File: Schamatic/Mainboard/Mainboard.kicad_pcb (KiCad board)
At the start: 2 copper layers, 45 x 130 mm, 277 parts, among them J1 CONN_01X02, J10 CONN_01X04, J2 CONN_01X02, J3 CONN_01X02, J4 CONN_01X02, J5 CONN_01X02, J6 CONN_02X05, J7 CONN_02X20, J8 CONN_01X02, J9 CONN_01X02, Q1 Q_NMOS_GDS, Q2 PSMN014-40YS, U1 LM2678-3.3V, U10 LTC2954, U2 LM2678-5V, U3 MC78M00, U4 LM5122, U5 UCC27611, U6 ACS781, U7 LSM6DS33, U8 STM32F031G6U6, U9 LTC2876, Y1 Resonator_Small

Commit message: changes
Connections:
- Y1 pad 2: (no net) -> Earth
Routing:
- net +BATT: track 200.3 -> 195.4 mm
- net 3.3V: track 250.1 -> 250.6 mm
- net Earth: vias 0 -> 1
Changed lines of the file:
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@@
 (kicad_pcb (version 4) (host pcbnew 4.0.6)
   (general
-    (links 0)
-    (no_connects 1)
-    (area 44.8 37.5 99.558572 172.600001)
+    (links 460)
+    (no_connects 2)
+    (area 49.924999 39.924999 95.075001 170.075001)
     (thickness 1.6)
     (drawings 4)
-    (tracks 1029)
+    (tracks 1034)
     (zones 0)
     (modules 277)
@@
     (47 F.CrtYd user)
     (48 B.Fab user)
-    (49 F.Fab user hide)
+    (49 F.Fab user)
   )
   (setup
-    (last_trace_width 0.13)
+    (last_trace_width 0.25)
     (user_trace_width 0.13)
     (user_trace_width 0.25)
@@
     (pad 1 smd rect (at 0 2.3 270) (size 0.4 1.4) (layers F.Cu F.Paste F.Mask)
       (net 50 "Net-(U8-Pad2)"))
-    (pad 2 smd rect (at 1.2 2.3 270) (size 0.4 1.4) (layers F.Cu F.Paste F.Mask))
+    (pad 2 smd rect (at 1.2 2.3 270) (size 0.4 1.4) (layers F.Cu F.Paste F.Mask)
+      (net 1 Earth))
     (pad 3 smd rect (at 2.4 2.3 270) (size 0.4 1.4) (layers F.Cu F.Paste F.Mask)
       (net 51 "Net-(U8-Pad3)"))
@@
   (gr_line (start 95 40) (end 95 170) (layer Edge.Cuts) (width 0.15))
   (gr_line (start 50 40) (end 95 40) (layer Edge.Cuts) (width 0.15))
+  (via (at 59.3 69.5) (size 0.4) (drill 0.25) (layers F.Cu B.Cu) (net 1))
   (segment (start 74.5 149.8) (end 74.5 149.58) (width 0.13) (layer F.Cu) (net 1))
   (segment (start 74.5 149.58) (end 74.8 149.28) (width 0.13) (layer F.Cu) (net 1))
@@
   (segment (start 58.725 149.5) (end 59.615 150.39) (width 0.25) (layer F.Cu) (net 3))
   (segment (start 59.615 150.39) (end 60.4 150.39) (width 0.25) (layer F.Cu) (net 3))
+  (segment (start 53.4 157.7) (end 53.4 144.75) (width 2) (layer B.Cu) (net 4))
+  (segment (start 53.4 144.75) (end 53.4 110.6) (width 2) (layer B.Cu) (net 4))
+  (segment (start 59.5 144.8) (end 53.45 144.8) (width 0.25) (layer B.Cu) (net 4))
+  (segment (start 53.45 144.8) (end 53.4 144.75) (width 0.25) (layer B.Cu) (net 4))
   (segment (start 88.4 113.6) (end 77.834602 113.6) (width 0.13) (layer F.Cu) (net 4))
   (segment (start 73.345001 113.645001) (end 70.499999 110.799999) (width 0.13) (layer F.Cu) (net 4))
@@
   (via (at 53.4 108.6) (size 0.4) (drill 0.25) (layers F.Cu B.Cu) (net 4))
   (via (at 53.4 109.6) (size 0.4) (drill 0.25) (layers F.Cu B.Cu) (net 4))
-  (segment (start 59.5 144.8) (end 53.2 138.5) (width 0.13) (layer B.Cu) (net 4))
-  (segment (start 53.2 138.5) (end 53.2 136.4) (width 0.13) (layer B.Cu) (net 4))
   (segment (start 64.22 144.28) (end 63.654999 144.845001) (width 0.13) (layer F.Cu) (net 4))
   (segment (start 63.654999 144.845001) (end 59.545001 144.845001) (width 0.13) (layer F.Cu) (net 4))
@@
   (segment (start 70.3 106) (end 70.2 105.9) (width 2) (layer F.Cu) (net 4))
   (via (at 70.3 110.6) (size 0.4) (drill 0.25) (layers F.Cu B.Cu) (net 4))
-  (segment (start 53.4 157.7) (end 53.4 110.6) (width 2) (layer B.Cu) (net 4))
   (via (at 53.4 110.6) (size 0.4) (drill 0.25) (layers F.Cu B.Cu) (net 4))
   (segment (start 61.5 165.8) (end 53.4 157.7) (width 2) (layer B.Cu) (net 4))
@@
   (segment (start 74.1 144.7) (end 74.1 146.4) (width 0.25) (layer F.Cu) (net 12))
   (segment (start 74.1 146.4) (end 74 146.5) (width 0.25) (layer F.Cu) (net 12))
+  (segment (start 78 97.6) (end 76.5 97.6) (width 0.25) (layer F.Cu) (net 13))
+  (segment (start 76.5 97.6) (end 76.05 98.05) (width 0.25) (layer F.Cu) (net 13))
+  (segment (start 76.05 98.05) (end 76.05 101.05) (width 0.25) (layer F.Cu) (net 13))
+  (segment (start 76.05 101.05) (end 75.4 101.7) (width 0.25) (layer F.Cu) (net 13))
+  (segment (start 75.4 101.7) (end 75.4 101.9) (width 0.25) (layer F.Cu) (net 13))
   (segment (start 85.119999 99.414978) (end 83.70502 97.999999) (width 0.25) (layer F.Cu) (net 13))
   (segment (start 88.9 103.35) (end 86.425001 100.875001) (width 0.25) (layer F.Cu) (net 13))
@@
   (segment (start 65.785161 75.799991) (end 64.93018 74.94501) (width 0.5) (layer B.Cu) (net 13))
   (segment (start 78 97.6) (end 77.7 97.6) (width 0.5) (layer F.Cu) (net 13))
-  (segment (start 77.7 97.6) (end 76.5 98.8) (width 0.5) (layer F.Cu) (net 13))
-  (segment (start 76.5 98.8) (end 76.5 101.5) (width 0.5) (layer F.Cu) (net 13))
-  (segment (start 76.5 101.5) (end 76.1 101.9) (width 0.5) (layer F.Cu) (net 13))
-  (segment (start 76.1 101.9) (end 75.4 101.9) (width 0.5) (layer F.Cu) (net 13))
   (segment (start 80.45 90.8) (end 80.45 85.91) (width 2) (layer F.Cu) (net 13))
   (segment (start 80.45 85.91) (end 77.84 83.3) (width 2) (layer F.Cu) (net 13))
@@
   (segment (start 75.7 62.035) (end 75.7 62.6) (width 0.5) (layer F.Cu) (net 13))
   (segment (start 88.025 72.18) (end 86.95 72.18) (width 0.5) (layer F.Cu) (net 13))
+  (segment (start 59.7 100.45) (end 59.594999 100.555001) (width 0.25) (layer F.Cu) (net 14))
+  (segment (start 59.594999 100.555001) (end 59.594999 100.905001) (width 0.25) (layer F.Cu) (net 14))
+  (segment (start 59.594999 100.905001) (end 58.8 101.7) (width 0.25) (layer F.Cu) (net 14))
   (segment (start 61.1 98.3) (end 61.1 99.05) (width 0.25) (layer F.Cu) (net 14))
   (segment (start 61.1 99.05) (end 59.7 100.45) (width 0.25) (layer F.Cu) (net 14))
-  (segment (start 59.7 100.8) (end 58.8 101.7) (width 0.25) (layer F.Cu) (net 14))
-  (segment (start 59.7 100.45) (end 59.7 100.8) (width 0.25) (layer F.Cu) (net 14))
   (segment (start 58.8 101.7) (end 58.8 101.9) (width 0.25) (layer F.Cu) (net 14))
   (segment (start 64.8 90.8) (end 64.8 86.3) (width 2) (layer F.Cu) (net 14))
@@
   (segment (start 89.25 108.05) (end 90.7 106.6) (width 0.13) (layer F.Cu) (net 56))
   (segment (start 90.7 106.6) (end 90.9 106.6) (width 0.13) (layer F.Cu) (net 56))
+  (segment (start 75.4 97.3) (end 75.85 97.75) (width 0.13) (layer B.Cu) (net 57))
+  (segment (start 75.85 97.75) (end 75.85 108.85) (width 0.13) (layer B.Cu) (net 57))
+  (segment (start 75.85 108.85) (end 72.899999 111.800001) (width 0.13) (layer B.Cu) (net 57))
+  (segment (start 72.899999 111.800001) (end 72.7 112) (width 0.13) (layer B.Cu) (net 57))
   (segment (start 85.545002 112.689602) (end 85.334605 112.899999) (width 0.13) (layer F.Cu) (net 57))
-  (segment (start 75.4 97.3) (end 75.4 109.3) (width 0.13) (layer B.Cu) (net 57))
   (segment (start 87.774206 107.589602) (end 86.895002 107.589602) (width 0.13) (layer F.Cu) (net 57))
   (segment (start 88.25 108.065396) (end 87.774206 107.589602) (width 0.13) (layer F.Cu) (net 57))
-  (segment (start 72.899999 111.800001) (end 72.7 112) (width 0.13) (layer B.Cu) (net 57))
-  (segment (start 75.4 109.3) (end 72.899999 111.800001) (width 0.13) (layer B.Cu) (net 57))
   (segment (start 88.25 109.2) (end 88.25 108.065396) (width 0.13) (layer F.Cu) (net 57))
   (segment (start 72.500001 112.199999) (end 72.7 112) (width 0.13) (layer B.Cu) (net 57))

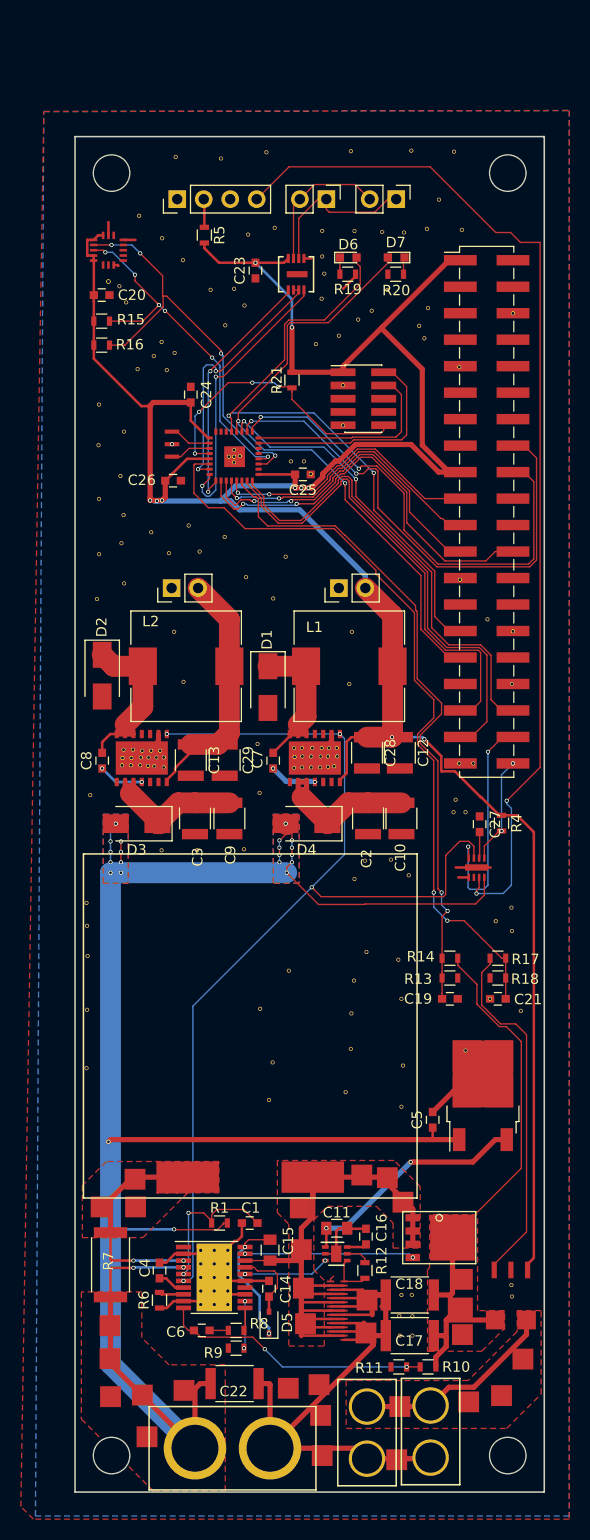
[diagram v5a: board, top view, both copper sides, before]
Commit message: mainboard plain MOSFETS
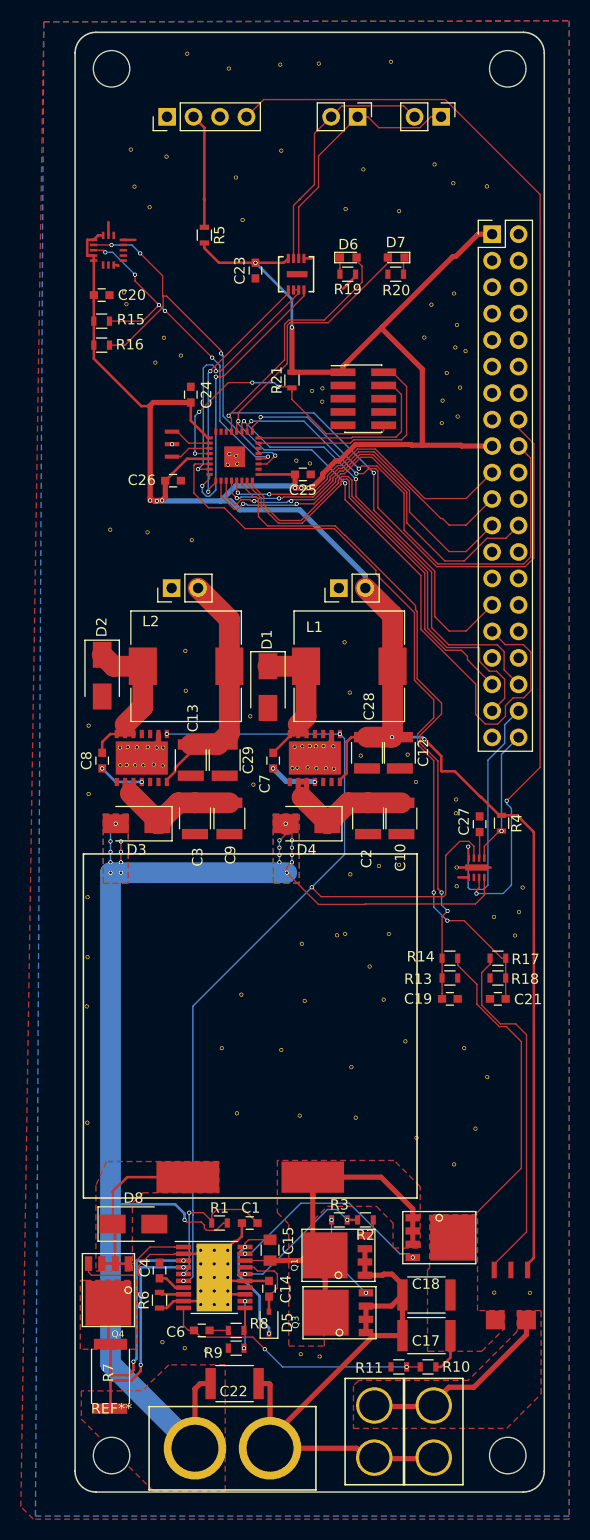
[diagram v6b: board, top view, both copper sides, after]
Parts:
- removed ? (x30): , Dizzy:2x2mm-pad
- removed C11: 2uF, Capacitors_SMD:C_0805
- removed C16: 2uF, Capacitors_SMD:C_0603
- removed C5: 1uF, Capacitors_SMD:C_0603
- removed R12: 10Ohm, Resistors_SMD:R_0603
- removed the REF** at (70.8, 71.2)
- removed the REF** at (51.2, 129.3)
- removed the REF** at (54.8, 98.8)
- removed the REF** at (55.6, 98.8)
- removed the REF** at (56.5, 98.9)
- removed the REF** at (57.4, 98.9)
- removed the REF** at (58.2, 98.9)
- removed the REF** at (75.0, 100.4)
- removed the REF** at (74.3, 100.5)
- removed the REF** at (73.6, 100.5)
- removed the REF** at (72.8, 100.5)
- removed the REF** at (71.8, 100.5)
- removed the REF** at (51.2, 123.8)
- removed the REF** at (71.1, 100.5)
- removed the REF** at (71.2, 99.5)
- removed the REF** at (71.9, 99.5)
- removed the REF** at (72.8, 99.5)
- removed the REF** at (73.7, 99.5)
- removed the REF** at (74.3, 99.5)
- removed the REF** at (75.2, 99.5)
- removed the REF** at (75.2, 98.7)
- removed the REF** at (74.5, 98.7)
- removed the REF** at (73.8, 98.7)
- removed the REF** at (51.3, 118.6)
- removed the REF** at (72.8, 98.7)
- removed the REF** at (71.8, 98.7)
- removed the REF** at (71.1, 98.7)
- removed the REF** at (87.0, 82.5)
- removed the REF** at (89.7, 86.3)
- removed the REF** at (92.1, 87.5)
- removed the REF** at (92.0, 92.5)
- removed the REF** at (88.3, 100.1)
- removed the REF** at (87.0, 100.1)
- removed the REF** at (87.5, 104.8)
- removed the REF** at (51.2, 115.7)
- removed the REF** at (86.6, 103.6)
- removed the REF** at (86.4, 104.8)
- removed the REF** at (82.1, 110.8)
- removed the REF** at (80.4, 109.3)
- removed the REF** at (77.9, 109.5)
- removed the REF** at (76.9, 111.2)
- removed the REF** at (92.0, 114.0)
- removed the REF** at (90.5, 115.2)
- removed the REF** at (92.0, 116.2)
- removed the REF** at (92.8, 123.8)
- removed the REF** at (51.2, 113.5)
- removed the REF** at (89.9, 122.7)
- removed the REF** at (70.6, 120.0)
- removed the REF** at (67.8, 123.7)
- removed the REF** at (69.0, 128.8)
- removed the REF** at (68.7, 132.4)
- removed the REF** at (76.0, 131.7)
- removed the REF** at (76.5, 127.5)
- removed the REF** at (76.6, 124.1)
- removed the REF** at (78.0, 118.2)
- removed the REF** at (81.1, 119.0)
- removed the REF** at (66.3, 108.3)
- removed the REF** at (76.8, 121.0)
- removed the REF** at (81.4, 122.7)
- removed the REF** at (81.5, 129.1)
- removed the REF** at (81.4, 133.1)
- removed the REF** at (81.2, 153.1)
- removed the REF** at (82.5, 153.2)
- removed the REF** at (82.5, 155.0)
- removed the REF** at (81.2, 155.0)
- removed the REF** at (82.4, 151.1)
- removed the REF** at (81.4, 151.1)
- removed the REF** at (61.8, 108.5)
- removed the REF** at (92.0, 151.2)
- removed the REF** at (92.0, 150.2)
- removed the REF** at (91.5, 43.5)
- removed the REF** at (53.5, 43.5)
- removed the REF** at (87.5, 127.7)
- removed the REF** at (58.4, 108.5)
- removed the REF** at (67.8, 103.0)
- removed the REF** at (67.6, 98.2)
- removed the REF** at (72.0, 71.2)
- removed the REF** at (76.4, 92.5)
- removed the REF** at (76.7, 87.5)
- removed the REF** at (59.6, 87.5)
- removed the REF** at (60.5, 92.3)
- removed the REF** at (69.1, 84.3)
- removed the REF** at (70.3, 80.3)
- removed the REF** at (66.5, 82.2)
- removed the REF** at (62.0, 79.8)
- removed the REF** at (59.1, 80.0)
- removed the REF** at (64.5, 78.4)
- removed the REF** at (72.7, 72.3)
- removed the REF** at (61.0, 77.3)
- removed the REF** at (57.4, 78.0)
- removed the REF** at (54.8, 68.3)
- removed the REF** at (54.5, 72.5)
- removed the REF** at (54.8, 76.3)
- removed the REF** at (54.5, 79.0)
- removed the REF** at (54.8, 82.8)
- removed the REF** at (52.2, 84.3)
- removed the REF** at (52.4, 80.0)
- removed the REF** at (52.4, 74.8)
- removed the REF** at (87.0, 62.1)
- removed the REF** at (52.4, 69.6)
- removed the REF** at (52.4, 65.7)
- removed the REF** at (57.6, 61.0)
- removed the REF** at (59.6, 60.8)
- removed the REF** at (56.1, 62.3)
- removed the REF** at (58.9, 62.4)
- removed the REF** at (58.4, 59.7)
- removed the REF** at (53.3, 53.9) (x2)
- removed the REF** at (54.4, 54.4)
- removed the REF** at (92.1, 57.0)
- removed the REF** at (55.0, 55.9)
- removed the REF** at (86.5, 41.5)
- removed the REF** at (82.3, 41.4)
- removed the REF** at (76.5, 41.4)
- removed the REF** at (68.5, 41.5)
- removed the REF** at (64.1, 42.1)
- removed the REF** at (59.8, 42.0)
- removed the REF** at (56.2, 47.6)
- removed the REF** at (69.2, 48.8)
- removed the REF** at (66.7, 49.4)
- removed the REF** at (84.0, 56.5)
- removed the REF** at (58.5, 49.8)
- removed the REF** at (60.5, 51.9)
- removed the REF** at (63.1, 54.7)
- removed the REF** at (65.3, 54.6)
- removed the REF** at (66.3, 56.2)
- removed the REF** at (64.5, 58.1)
- removed the REF** at (87.2, 49.0)
- removed the REF** at (85.0, 46.0)
- removed the REF** at (83.8, 48.9)
- removed the REF** at (81.7, 49.2)
- removed the REF** at (83.6, 59.4)
- removed the REF** at (79.5, 49.1)
- removed the REF** at (76.9, 49.0)
- removed the REF** at (73.8, 49.0)
- removed the REF** at (73.8, 51.5)
- removed the REF** at (74.0, 53.1)
- removed the REF** at (73.8, 55.5)
- removed the REF** at (73.2, 59.9)
- removed the REF** at (75.4, 59.1)
- removed the REF** at (77.2, 57.5)
- removed the REF** at (78.5, 56.7)
- removed the REF** at (83.1, 58.1)
- removed the REF** at (80.0, 54.7)
- removed the REF** at (75.8, 67.7)
- removed the REF** at (75.8, 63.9)
- removed the REF** at (65.3, 70.0)
- removed the REF** at (65.3, 71.2)
- removed the REF** at (65.9, 70.7)
- removed the REF** at (64.8, 70.7)
- removed the REF** at (65.3, 70.7)
- removed the REF** at (54.6, 100.3)
- removed the REF** at (55.5, 100.3)
- removed the REF** at (51.5, 103.2)
- removed the REF** at (56.4, 100.3)
- removed the REF** at (57.1, 100.3)
- removed the REF** at (57.7, 100.4)
- removed the REF** at (58.6, 100.5)
- removed the REF** at (58.6, 99.5)
- removed the REF** at (57.9, 99.5)
- removed the REF** at (57.1, 99.5)
- removed the REF** at (56.4, 99.5)
- removed the REF** at (55.5, 99.6)
- removed the REF** at (54.6, 99.6)
- removed U3: MC78M00, TO_SOT_Packages_SMD:TO-252-2
- removed U5: UCC27611, Housings_DFN_QFN:DFN-6-1EP_2x2mm_Pitch0.65mm
- added D8: D_Small, Diodes_SMD:D_SMA, F.Cu at (55.6, 144.3)
- added Q3: PSMN014-40YS, Dizzy:PSMN3R3-40YS, F.Cu at (75.4, 152.8)
- added Q4: PSMN014-40YS, Dizzy:PSMN3R3-40YS, F.Cu at (53.2, 150.6)
- added R2: 10Ohm, Resistors_SMD:R_0603, F.Cu at (77.8, 143.9)
- added R3: 10Ohm, Resistors_SMD:R_0603, F.Cu at (75.3, 143.9)
- added REF**: VIA-0.4, Dizzy:VIA-0.4, F.Cu at (86.7, 110.1)
- added REF**: VIA-0.4, Dizzy:VIA-0.4, F.Cu at (57.9, 98.6)
- added REF**: VIA-0.4, Dizzy:VIA-0.4, F.Cu at (81.2, 47.1)
- added REF**: VIA-0.4, Dizzy:VIA-0.4, F.Cu at (86.5, 55.0)
- added REF**: VIA-0.4, Dizzy:VIA-0.4, F.Cu at (84.3, 56.1)
- added REF**: VIA-0.4, Dizzy:VIA-0.4, F.Cu at (83.6, 59.3)
- added REF**: VIA-0.4, Dizzy:VIA-0.4, F.Cu at (86.7, 58.1)
- added REF**: VIA-0.4, Dizzy:VIA-0.4, F.Cu at (86.6, 60.2)
- added REF**: VIA-0.4, Dizzy:VIA-0.4, F.Cu at (87.5, 60.6)
- added REF**: VIA-0.4, Dizzy:VIA-0.4, F.Cu at (85.8, 62.7)
- added REF**: VIA-0.4, Dizzy:VIA-0.4, F.Cu at (87.0, 64.1)
- added REF**: VIA-0.4, Dizzy:VIA-0.4, F.Cu at (85.3, 65.3)
- added REF**: VIA-0.4, Dizzy:VIA-0.4, F.Cu at (57.1, 98.5)
- added REF**: VIA-0.4, Dizzy:VIA-0.4, F.Cu at (86.8, 66.8)
- added REF**: VIA-0.4, Dizzy:VIA-0.4, F.Cu at (85.3, 67.5)
- added REF**: VIA-0.4, Dizzy:VIA-0.4, F.Cu at (73.8, 65.4)
- added REF**: VIA-0.4, Dizzy:VIA-0.4, F.Cu at (73.8, 64.2)
- added REF**: VIA-0.4, Dizzy:VIA-0.4, F.Cu at (72.8, 64.4)
- added REF**: VIA-0.4, Dizzy:VIA-0.4, F.Cu at (71.3, 71.1)
- added REF**: VIA-0.4, Dizzy:VIA-0.4, F.Cu at (72.6, 71.3)
- added REF**: VIA-0.4, Dizzy:VIA-0.4, F.Cu at (65.5, 70.6)
- added REF**: VIA-0.4, Dizzy:VIA-0.4, F.Cu at (64.9, 70.5)
- added REF**: VIA-0.4, Dizzy:VIA-0.4, F.Cu at (65.7, 71.4)
- added REF**: VIA-0.4, Dizzy:VIA-0.4, F.Cu at (56.0, 98.6)
- added REF**: VIA-0.4, Dizzy:VIA-0.4, F.Cu at (64.8, 71.5)
- added REF**: VIA-0.4, Dizzy:VIA-0.4, F.Cu at (61.3, 78.7)
- added REF**: VIA-0.4, Dizzy:VIA-0.4, F.Cu at (57.0, 78.0)
- added REF**: MountingHole_3.5mm, Mounting_Holes:MountingHole_3.5mm, F.Cu at (91.5, 33.5)
- added REF**: MountingHole_3.5mm, Mounting_Holes:MountingHole_3.5mm, F.Cu at (53.5, 33.5)
- added REF**: VIA-0.4, Dizzy:VIA-0.4, F.Cu at (53.5, 77.7)
- added REF**: VIA-0.4, Dizzy:VIA-0.4, F.Cu at (55.1, 98.5)
- added REF**: VIA-0.4, Dizzy:VIA-0.4, F.Cu at (54.4, 98.6)
- added REF**: VIA-0.4, Dizzy:VIA-0.4, F.Cu at (71.0, 100.6)
- added REF**: VIA-0.4, Dizzy:VIA-0.4, F.Cu at (71.4, 100.5)
- added REF**: VIA-0.4, Dizzy:VIA-0.4, F.Cu at (72.4, 100.5)
- added REF**: VIA-0.4, Dizzy:VIA-0.4, F.Cu at (73.2, 100.6)
- added REF**: VIA-0.4, Dizzy:VIA-0.4, F.Cu at (74.2, 100.6)
- added REF**: VIA-0.4, Dizzy:VIA-0.4, F.Cu at (86.7, 111.9)
- added REF**: VIA-0.4, Dizzy:VIA-0.4, F.Cu at (74.9, 100.6)
- added REF**: VIA-0.4, Dizzy:VIA-0.4, F.Cu at (74.9, 98.5)
- added REF**: VIA-0.4, Dizzy:VIA-0.4, F.Cu at (73.9, 98.5)
- added REF**: VIA-0.4, Dizzy:VIA-0.4, F.Cu at (73.2, 98.5)
- added REF**: VIA-0.4, Dizzy:VIA-0.4, F.Cu at (72.6, 98.5)
- added REF**: VIA-0.4, Dizzy:VIA-0.4, F.Cu at (71.9, 98.5)
- added REF**: VIA-0.4, Dizzy:VIA-0.4, F.Cu at (71.2, 98.5)
- added REF**: VIA-0.4, Dizzy:VIA-0.4, F.Cu at (77.5, 99.4)
- added REF**: VIA-0.4, Dizzy:VIA-0.4, F.Cu at (82.0, 99.3)
- added REF**: VIA-0.4, Dizzy:VIA-0.4, F.Cu at (82.8, 101.9)
- added REF**: VIA-0.4, Dizzy:VIA-0.4, F.Cu at (54.5, 100.3)
- added REF**: VIA-0.4, Dizzy:VIA-0.4, F.Cu at (73.5, 157.0)
- added REF**: VIA-0.4, Dizzy:VIA-0.4, F.Cu at (71.8, 156.8)
- added REF**: VIA-0.4, Dizzy:VIA-0.4, F.Cu at (62.7, 156.4)
- added REF**: VIA-0.4, Dizzy:VIA-0.4, F.Cu at (60.6, 156.2)
- added REF**: VIA-0.4, Dizzy:VIA-0.4, F.Cu at (58.5, 155.6)
- added REF**: VIA-0.4, Dizzy:VIA-0.4, F.Cu at (90.3, 150.9)
- added REF**: VIA-0.4, Dizzy:VIA-0.4, F.Cu at (93.7, 150.9)
- added REF**: VIA-0.4, Dizzy:VIA-0.4, F.Cu at (58.6, 59.3)
- added REF**: VIA-0.4, Dizzy:VIA-0.4, F.Cu at (60.2, 61.0)
- added REF**: VIA-0.4, Dizzy:VIA-0.4, F.Cu at (57.8, 61.7)
- added REF**: VIA-0.4, Dizzy:VIA-0.4, F.Cu at (55.0, 100.3)
- added REF**: VIA-0.4, Dizzy:VIA-0.4, F.Cu at (67.2, 102.2)
- added REF**: VIA-0.4, Dizzy:VIA-0.4, F.Cu at (66.9, 95.6)
- added REF**: VIA-0.4, Dizzy:VIA-0.4, F.Cu at (76.0, 88.5)
- added REF**: VIA-0.4, Dizzy:VIA-0.4, F.Cu at (76.5, 93.3)
- added REF**: VIA-0.4, Dizzy:VIA-0.4, F.Cu at (60.7, 89.3)
- added REF**: VIA-0.4, Dizzy:VIA-0.4, F.Cu at (60.7, 93.2)
- added REF**: VIA-0.4, Dizzy:VIA-0.4, F.Cu at (51.4, 96.5)
- added REF**: VIA-0.4, Dizzy:VIA-0.4, F.Cu at (51.4, 103.0)
- added REF**: VIA-0.4, Dizzy:VIA-0.4, F.Cu at (51.3, 134.6)
- added REF**: VIA-0.4, Dizzy:VIA-0.4, F.Cu at (51.3, 113.0)
- added REF**: VIA-0.4, Dizzy:VIA-0.4, F.Cu at (55.9, 100.3)
- added REF**: VIA-0.4, Dizzy:VIA-0.4, F.Cu at (51.3, 118.7)
- added REF**: VIA-0.4, Dizzy:VIA-0.4, F.Cu at (51.2, 123.4)
- added REF**: VIA-0.4, Dizzy:VIA-0.4, F.Cu at (76.6, 129.2)
- added REF**: VIA-0.4, Dizzy:VIA-0.4, F.Cu at (72.1, 122.9)
- added REF**: VIA-0.4, Dizzy:VIA-0.4, F.Cu at (69.9, 127.6)
- added REF**: VIA-0.4, Dizzy:VIA-0.4, F.Cu at (78.3, 119.6)
- added REF**: VIA-0.4, Dizzy:VIA-0.4, F.Cu at (79.7, 122.8)
- added REF**: VIA-0.4, Dizzy:VIA-0.4, F.Cu at (81.8, 126.8)
- added REF**: VIA-0.4, Dizzy:VIA-0.4, F.Cu at (87.4, 127.4)
- added REF**: VIA-0.4, Dizzy:VIA-0.4, F.Cu at (89.6, 130.2)
- added REF**: VIA-0.4, Dizzy:VIA-0.4, F.Cu at (56.6, 100.3)
- added REF**: VIA-0.4, Dizzy:VIA-0.4, F.Cu at (88.5, 135.2)
- added REF**: VIA-0.4, Dizzy:VIA-0.4, F.Cu at (86.5, 138.6)
- added REF**: VIA-0.4, Dizzy:VIA-0.4, F.Cu at (82.8, 136.0)
- added REF**: VIA-0.4, Dizzy:VIA-0.4, F.Cu at (77.0, 134.1)
- added REF**: VIA-0.4, Dizzy:VIA-0.4, F.Cu at (71.7, 133.9)
- added REF**: VIA-0.4, Dizzy:VIA-0.4, F.Cu at (65.6, 133.7)
- added REF**: VIA-0.4, Dizzy:VIA-0.4, F.Cu at (64.2, 127.4)
- added REF**: VIA-0.4, Dizzy:VIA-0.4, F.Cu at (66.0, 122.3)
- added REF**: VIA-0.4, Dizzy:VIA-0.4, F.Cu at (71.8, 117.4)
- added REF**: VIA-0.4, Dizzy:VIA-0.4, F.Cu at (75.2, 116.6)
- added REF**: VIA-0.4, Dizzy:VIA-0.4, F.Cu at (57.6, 100.2)
- added REF**: VIA-0.4, Dizzy:VIA-0.4, F.Cu at (76.0, 116.5)
- added REF**: VIA-0.4, Dizzy:VIA-0.4, F.Cu at (80.2, 116.5)
- added REF**: VIA-0.4, Dizzy:VIA-0.4, F.Cu at (92.3, 116.6)
- added REF**: VIA-0.4, Dizzy:VIA-0.4, F.Cu at (90.3, 114.8)
- added REF**: VIA-0.4, Dizzy:VIA-0.4, F.Cu at (92.7, 114.4)
- added REF**: VIA-0.4, Dizzy:VIA-0.4, F.Cu at (93.0, 112.0)
- added REF**: VIA-0.4, Dizzy:VIA-0.4, F.Cu at (76.5, 110.8)
- added REF**: VIA-0.4, Dizzy:VIA-0.4, F.Cu at (79.2, 110.0)
- added REF**: VIA-0.4, Dizzy:VIA-0.4, F.Cu at (81.2, 109.8)
- added REF**: VIA-0.4, Dizzy:VIA-0.4, F.Cu at (86.6, 104.9)
- added REF**: VIA-0.4, Dizzy:VIA-0.4, F.Cu at (58.5, 100.3)
- added REF**: VIA-0.4, Dizzy:VIA-0.4, F.Cu at (86.7, 103.6)
- added REF**: VIA-0.4, Dizzy:VIA-0.4, F.Cu at (54.8, 55.0)
- added REF**: VIA-0.4, Dizzy:VIA-0.4, F.Cu at (55.0, 56.1)
- added REF**: VIA-0.4, Dizzy:VIA-0.4, F.Cu at (80.4, 32.8)
- added REF**: VIA-0.4, Dizzy:VIA-0.4, F.Cu at (73.5, 33.0)
- added REF**: VIA-0.4, Dizzy:VIA-0.4, F.Cu at (69.8, 33.1)
- added REF**: VIA-0.4, Dizzy:VIA-0.4, F.Cu at (64.8, 33.5)
- added REF**: VIA-0.4, Dizzy:VIA-0.4, F.Cu at (60.9, 32.0)
- added REF**: VIA-0.4, Dizzy:VIA-0.4, F.Cu at (58.9, 41.9)
- added REF**: VIA-0.4, Dizzy:VIA-0.4, F.Cu at (55.5, 41.2)
- added REF**: VIA-0.4, Dizzy:VIA-0.4, F.Cu at (58.5, 98.6)
- added REF**: VIA-0.4, Dizzy:VIA-0.4, F.Cu at (55.8, 44.8)
- added REF**: VIA-0.4, Dizzy:VIA-0.4, F.Cu at (57.2, 46.8)
- added REF**: VIA-0.4, Dizzy:VIA-0.4, F.Cu at (69.9, 41.4)
- added REF**: VIA-0.4, Dizzy:VIA-0.4, F.Cu at (65.5, 43.9)
- added REF**: VIA-0.4, Dizzy:VIA-0.4, F.Cu at (66.2, 48.0)
- added REF**: VIA-0.4, Dizzy:VIA-0.4, F.Cu at (89.6, 44.8)
- added REF**: VIA-0.4, Dizzy:VIA-0.4, F.Cu at (86.4, 44.5)
- added REF**: VIA-0.4, Dizzy:VIA-0.4, F.Cu at (84.6, 42.7)
- added REF**: VIA-0.4, Dizzy:VIA-0.4, F.Cu at (77.8, 43.1)
- added REF**: VIA-0.4, Dizzy:VIA-0.4, F.Cu at (76.0, 47.0)
- J7: footprint Pin_Headers:Pin_Header_Straight_2x20_Pitch2.54mm_SMD -> Pin_Headers:Pin_Header_Straight_2x20_Pitch2.54mm
- Q1: value Q_NMOS_GDS -> PSMN014-40YS; footprint Dizzy:EPC2022 -> Dizzy:PSMN3R3-40YS
- U4: value LM5122 -> LM5121
- moved J7 26.6 mm to (90.0, 49.4)
- moved R7 10.7 mm to (53.4, 158.9)
- moved Q1 9.68 mm to (75.3, 147.3), turned to 90 degrees
- moved J1 8.99 mm to (85.1, 38.1)
- moved J2 8.45 mm to (77.1, 38.1)
- moved J10 7.96 mm to (58.8, 38.1)
- moved C17 1.60 mm to (83.7, 155.0)
- moved C18 1.60 mm to (83.7, 151.1)
- moved J4 0.71 mm to (78.7, 164.2)
- moved J5 0.30 mm to (84.4, 164.2)
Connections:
- L3 pad 1: Net-(L3-Pad1) -> Net-(D8-Pad1)
- Q1 pad 1: Net-(Q1-Pad1) -> Earth
- Q1 pad 2: Net-(C15-Pad1) -> Earth
- R7 pad 1: Net-(L3-Pad1) -> Net-(Q4-Pad5678)
- U4 pad 1: (no net) -> Net-(D8-Pad1)
- U4 pad 2: Earth -> Net-(Q4-Pad4)
- U4 pad 3: Net-(L3-Pad1) -> Net-(Q4-Pad5678)
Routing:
- net +BATT: track 195.4 -> 156.7 mm, vias 23 -> 22
- net Earth: track 121.4 -> 90.3 mm
- net Net-(C15-Pad1): track 66.2 -> 38.1 mm
- net Net-(Q4-Pad5678): track 0.00 -> 24.6 mm, vias 0 -> 2
- net Net-(D8-Pad1): track 0.00 -> 23.3 mm
- net +18V: track 22.7 -> 0.00 mm, vias 2 -> 0
- net RECVRDY: track 59.6 -> 80.9 mm
- net Net-(L3-Pad1): track 21.2 -> 0.00 mm, vias 2 -> 0
- net Net-(C17-Pad1): track 53.1 -> 36.3 mm
- net Net-(Q4-Pad4): track 0.00 -> 12.7 mm
- net RS-A: track 14.0 -> 24.1 mm
- net RS-B: track 15.6 -> 24.8 mm
- net Net-(J10-Pad2): track 2.72 -> 11.1 mm
- net Net-(Q3-Pad4): track 0.00 -> 8.36 mm, vias 0 -> 2
- net PWR_BUTTON: track 100.0 -> 105.7 mm
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- added copper zone on F.Cu, net Net-(Q4-Pad5678)
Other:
- board size 45 x 130 mm -> 45 x 140 mm
- board text added: "+"
- board text added: "-"
- board text added: "12-24 V supply"
- board text added: "3.3V"
- board text added: "5V"
- board text added: "90 V output"
- board text added: "A"
- board text added: "B"
- board text added: "DizzyRobot"
- board text added: "GND"
- board text added: "LED"
- board text added: "RS485"
- board text added: "button"

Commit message: fixing schematic errors
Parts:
- C1: value 1uF -> 2.2uF
- C27: value 2.2uF -> 0.47uF
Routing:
- net Net-(Q4-Pad4): track 12.7 -> 11.4 mm
- net Earth: track 90.3 -> 89.4 mm
- added copper zone on F.Cu, net Net-(D8-Pad1)
- removed copper zone on F.Cu, net Net-(L3-Pad1)

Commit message: started linearization for A1335
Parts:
- C14, C4: value 0.47uF -> 1uF
- C27: value 0.47uF -> 0.33uF
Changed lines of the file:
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@@
     (47 F.CrtYd user)
     (48 B.Fab user)
-    (49 F.Fab user hide)
+    (49 F.Fab user)
   )
   (setup
@@
     (pad_to_mask_clearance 0.2)
     (aux_axis_origin 0 0)
-    (visible_elements 7FFFFFFF)
+    (visible_elements 7FFFEFFF)
     (pcbplotparams
       (layerselection 0x010f0_80000001)
@@
       (effects (font (size 1 1) (thickness 0.15)))
     )
-    (fp_text value 0.47uF (at 0 1.5 90) (layer F.Fab)
+    (fp_text value 1uF (at 0 1.5 90) (layer F.Fab)
       (effects (font (size 1 1) (thickness 0.15)))
     )
@@
       (effects (font (size 1 1) (thickness 0.15)))
     )
-    (fp_text value 0.47uF (at 0 1.5 90) (layer F.Fab)
+    (fp_text value 1uF (at 0 1.5 90) (layer F.Fab)
       (effects (font (size 1 1) (thickness 0.15)))
     )
@@
       (effects (font (size 1 1) (thickness 0.15)))
     )
-    (fp_text value 0.47uF (at 0 1.5 270) (layer F.Fab)
+    (fp_text value 0.33uF (at 0 1.5 270) (layer F.Fab)
       (effects (font (size 1 1) (thickness 0.15)))
     )
